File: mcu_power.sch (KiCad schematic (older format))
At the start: 20 parts

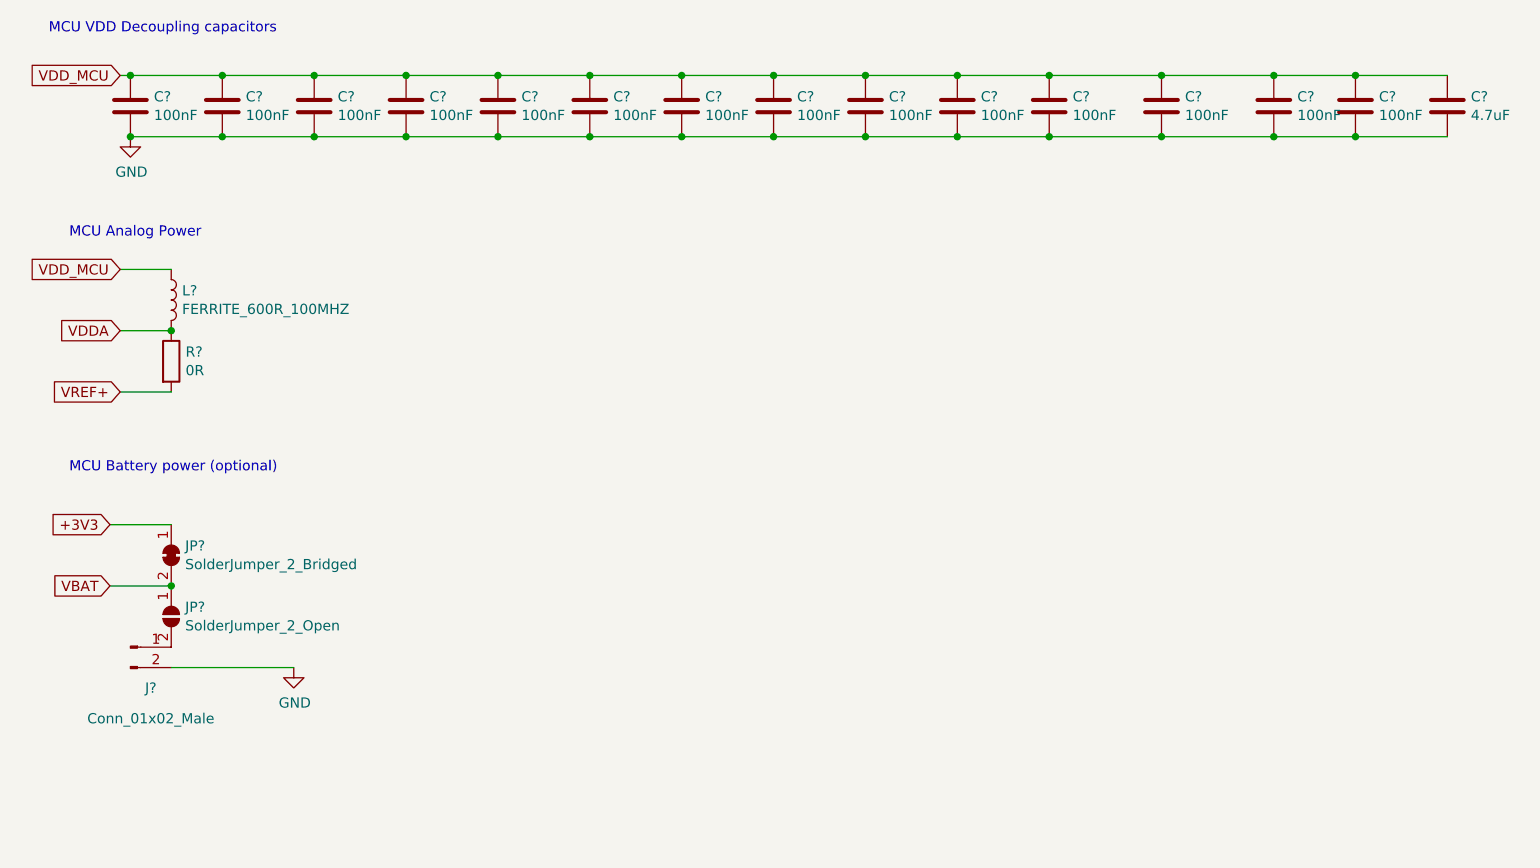
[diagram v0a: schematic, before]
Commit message: Finished MCU power, MCU crystals, started CODEC
Not done CODEC.

Where are the I2S BCLK and LRCLK?
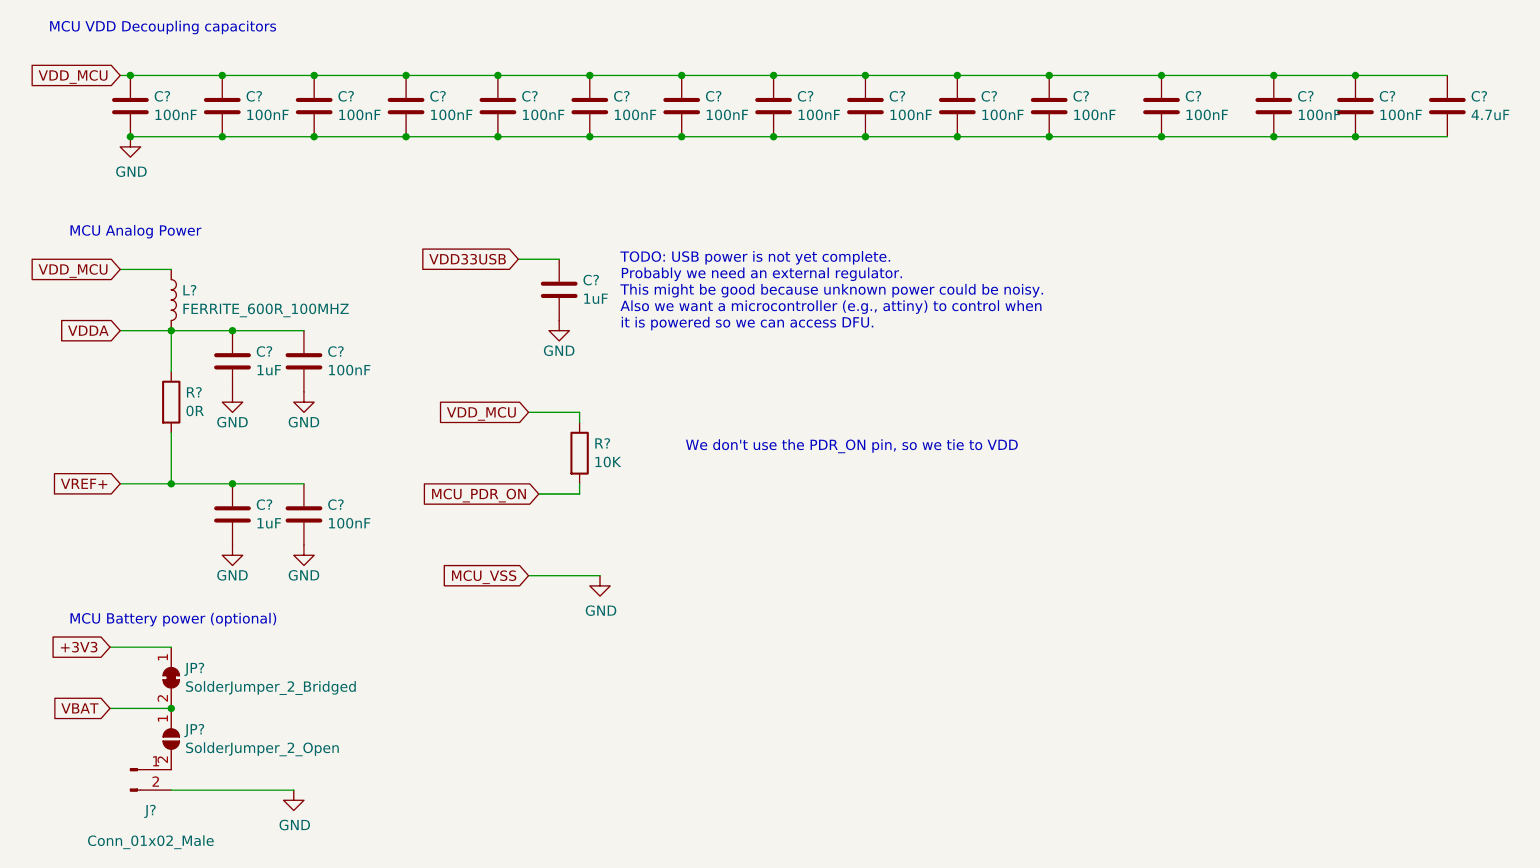
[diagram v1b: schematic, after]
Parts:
- added C? (x3): 1uF, symbol Device:C
- added C? (x2): 100nF, symbol Device:C
- added R?: 10K, symbol Device:R
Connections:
- net GND: now also C?.2, C?.2, C?.2, C?.2, C?.2
- net VDDA: now also C?.1, C?.1
- net VDD_MCU: now also R?.1
- net VREF+: now also C?.1, C?.1
- new net MCU_PDR_ON: R?.2
- new net VDD33USB: C?.1
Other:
- note added: "TODO: USB power is not yet complete.\nProbably we need an external regulator. \nThis might be good because unknown power could be noisy. \nAlso we want a microcontroller (e.g., attiny) to control when \nit is powered so we can access DFU."
- note added: "We don't use the PDR_ON pin, so we tie to VDD\n"
- moved on the sheet: J?, JP?, R?
